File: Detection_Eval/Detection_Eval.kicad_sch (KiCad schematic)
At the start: 13 parts, among them J1 USB_A, SW1 SW_Push, SW2 SW_Push, U1 ESP8266

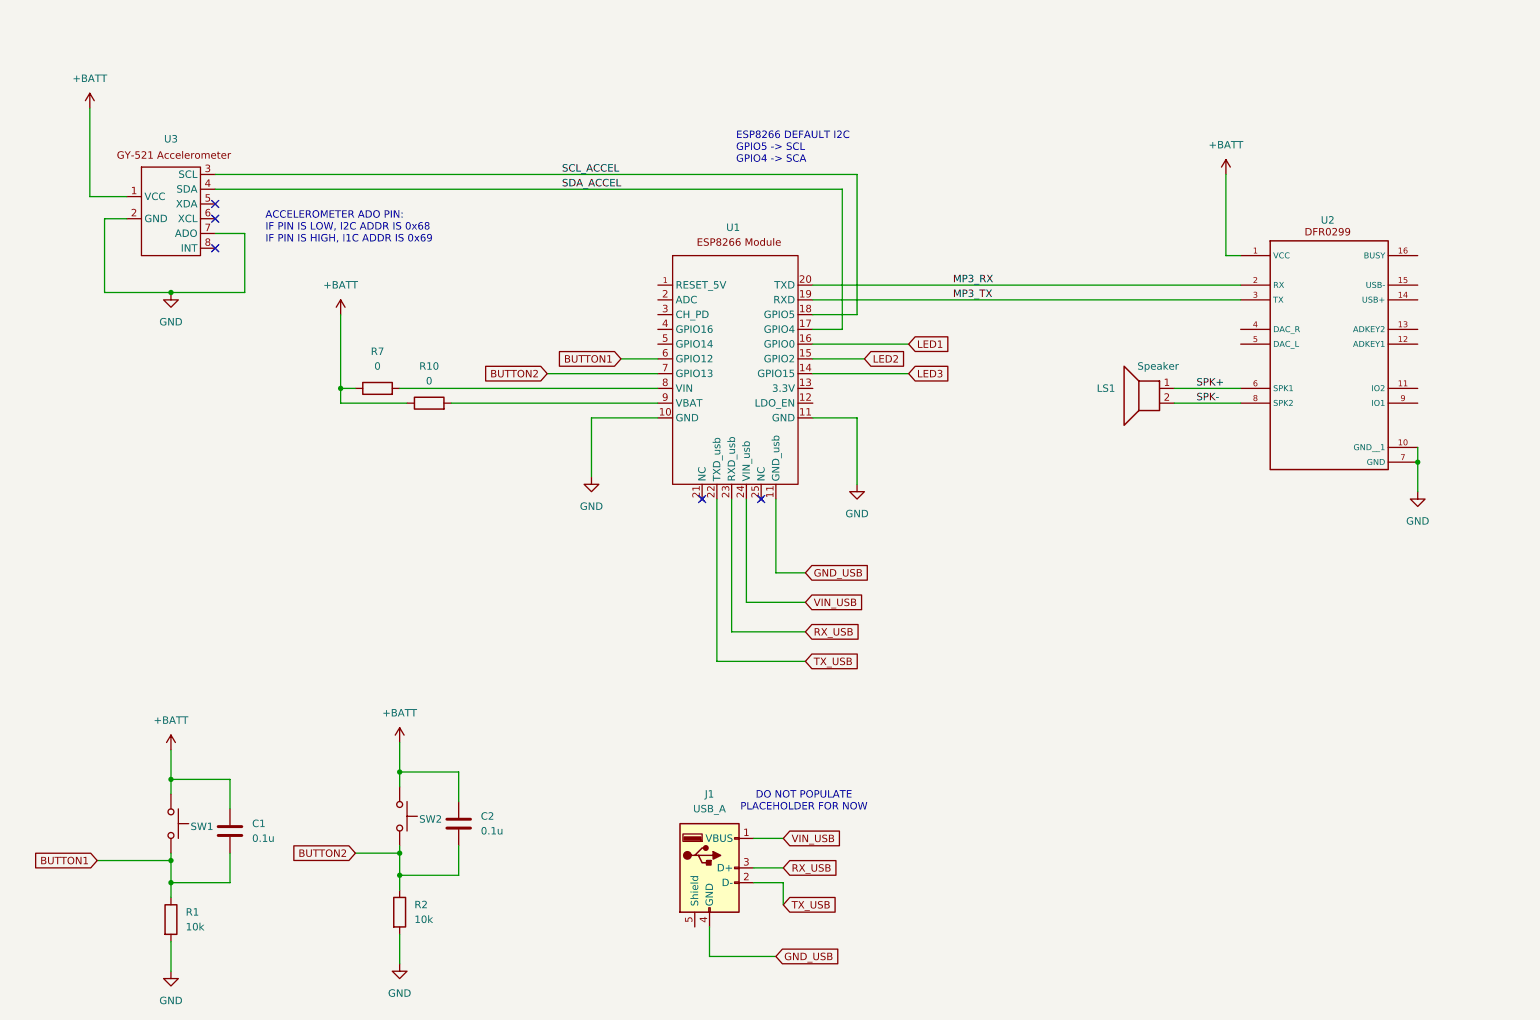
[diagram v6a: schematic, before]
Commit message: Madison_02-03_REV002
this is the begining of REV002
Added LCD, heartbeat monitor
Added page for ESP8266 and USB
Added AND failsafe circuit
Further page organization

NEEDS REVIEW
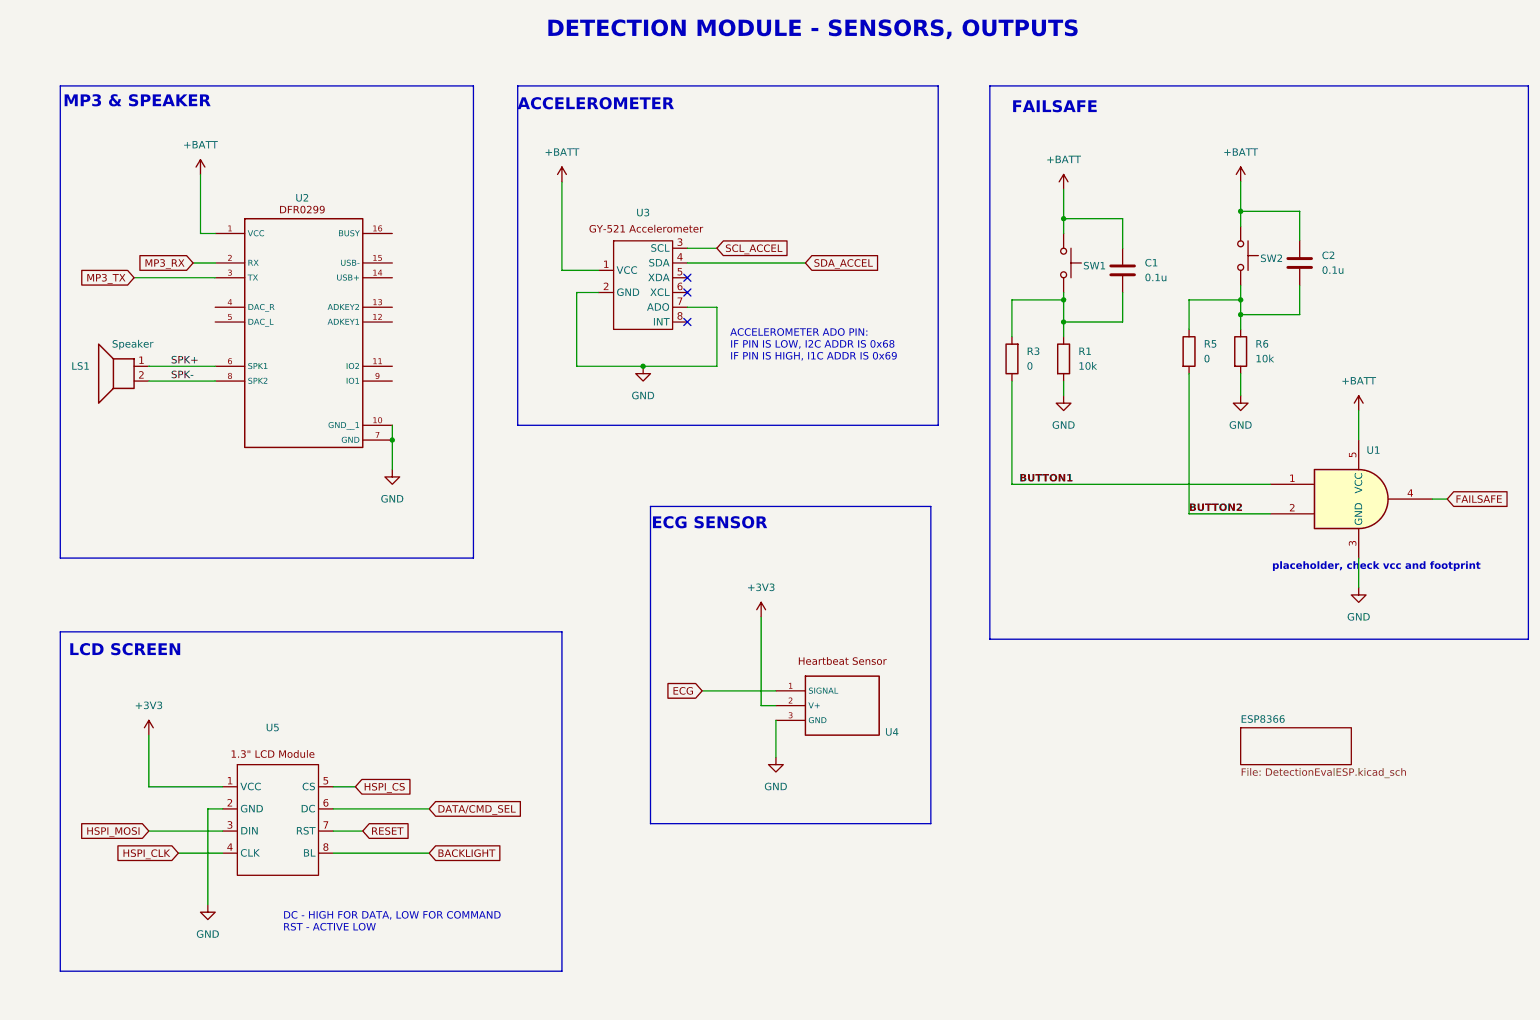
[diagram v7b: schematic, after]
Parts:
- removed J1: USB_A, symbol Connector:USB_A
- removed R10, R7: 0, Resistor_SMD:R_0402_1005Metric, symbol Device:R
- removed R2: 10k, Resistor_SMD:R_0402_1005Metric, symbol Device:R
- removed U1: ESP8266, symbol Detection_Eval_lib:ESP_Hold
- added R3, R5: 0, Resistor_SMD:R_0402_1005Metric, symbol Device:R
- added R6: 10k, Resistor_SMD:R_0402_1005Metric, symbol Device:R
- added U1: 74AHC1G08, symbol 74xGxx:74AHC1G08
- added U4: ~, Connector_PinHeader_2.54mm:PinHeader_1x03_P2.54mm_Horizontal, symbol Detection_Eval_lib:heartbeat
- added U5: ~, symbol Detection_Eval_lib:LCDModule
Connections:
- net +BATT: now also U1.5 (VCC)
- net BUTTON1: now also R3.1, U1.1; no longer C1.2, R1.1, SW1.2
- net BUTTON2: now also R5.2, U1.2; no longer C2.2, SW2.2
- net GND: now also R6.2, U1.3 (GND), U4.3 (GND), U5.2 (GND)
- new net: C1.2, R1.1, R3.2, SW1.2
- new net: C2.2, R5.1, R6.1, SW2.2
- new net +3V3: U4.2 (V+), U5.1 (VCC)
- new net BACKLIGHT: U5.8 (BL)
- new net DATA/CMD_SEL: U5.6 (DC)
- new net ECG: U4.1 (SIGNAL)
- new net FAILSAFE: U1.4
- new net HSPI_CLK: U5.4 (CLK)
- new net HSPI_CS: U5.5 (CS)
- new net HSPI_MOSI: U5.3 (DIN)
- new net RESET: U5.7 (RST)
- no-connect marks 5 -> 3
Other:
- added sheet ESP8366 (DetectionEvalESP.kicad_sch)
- note added: "ACCELEROMETER"
- note added: "DC - HIGH FOR DATA, LOW FOR COMMAND RST - ACTIVE LOW"
- note added: "DETECTION MODULE - SENSORS, OUTPUTS"
- note added: "ECG SENSOR"
- note added: "FAILSAFE"
- note added: "LCD SCREEN"
- note added: "MP3 & SPEAKER"
- note added: "placeholder, check vcc and footprint"
- note removed: "DO NOT POPULATE PLACEHOLDER FOR NOW"
- note removed: "ESP8266 DEFAULT I2C GPIO5 -> SCL GPIO4 -> SCA"
- moved on the sheet: C1, LS1, R1, SW1, U2, U3

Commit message: Madison_02-04
Battery added
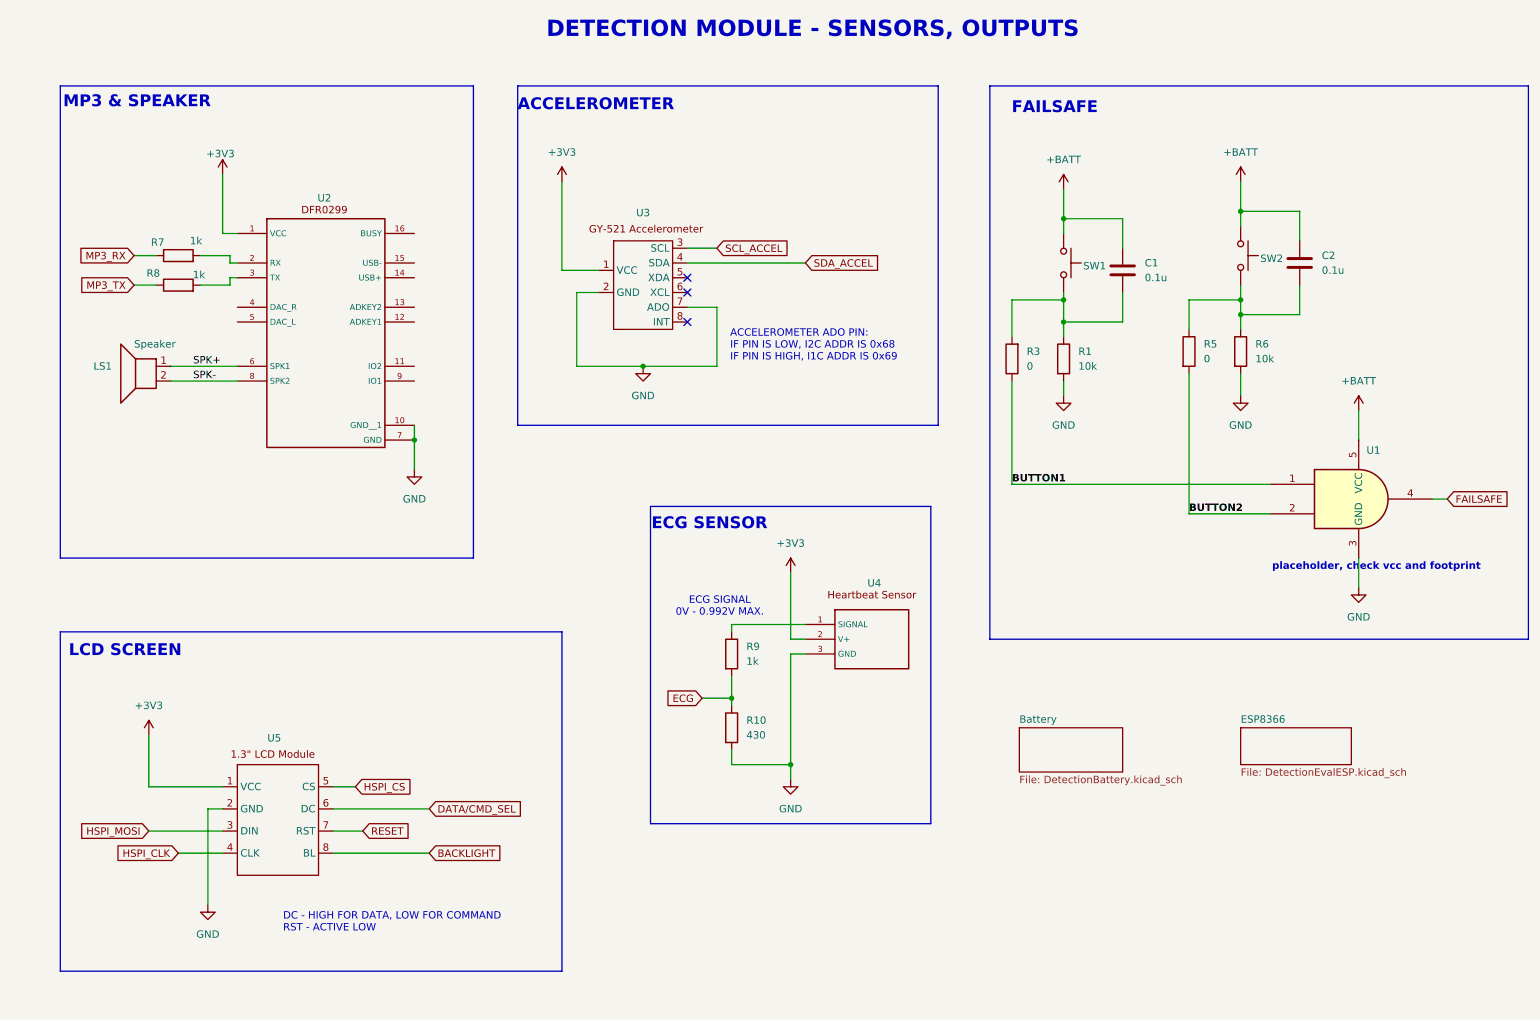
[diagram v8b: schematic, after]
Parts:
- added R10: 430, Resistor_SMD:R_0402_1005Metric, symbol Device:R
- added R7, R8, R9: 1k, Resistor_SMD:R_0402_1005Metric, symbol Device:R
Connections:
- net +3V3: now also U2.1 (VCC), U3.1 (VCC)
- net +BATT: no longer U2.1 (VCC), U3.1 (VCC)
- net ECG: now also R10.1, R9.2; no longer U4.1 (SIGNAL)
- net GND: now also R10.2
- net MP3_RX: now also R7.1; no longer U2.2 (RX)
- net MP3_TX: now also R8.1; no longer U2.3 (TX)
- new net: R7.2, U2.2 (RX)
- new net: R8.2, U2.3 (TX)
- new net: R9.1, U4.1 (SIGNAL)
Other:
- added sheet Battery (DetectionBattery.kicad_sch)
- note added: "ECG SIGNAL 0V - 0.992V MAX."
- moved on the sheet: LS1, U2, U4
